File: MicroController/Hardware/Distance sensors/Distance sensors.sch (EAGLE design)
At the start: 37 parts, among them U1 LM2937IMP-5.0, U2 TXB0108PWR, U3 TLV1117-33CDCY, U4 TXB0108PWR, X1 0446200002, X2 0446200002, X3 0446200002

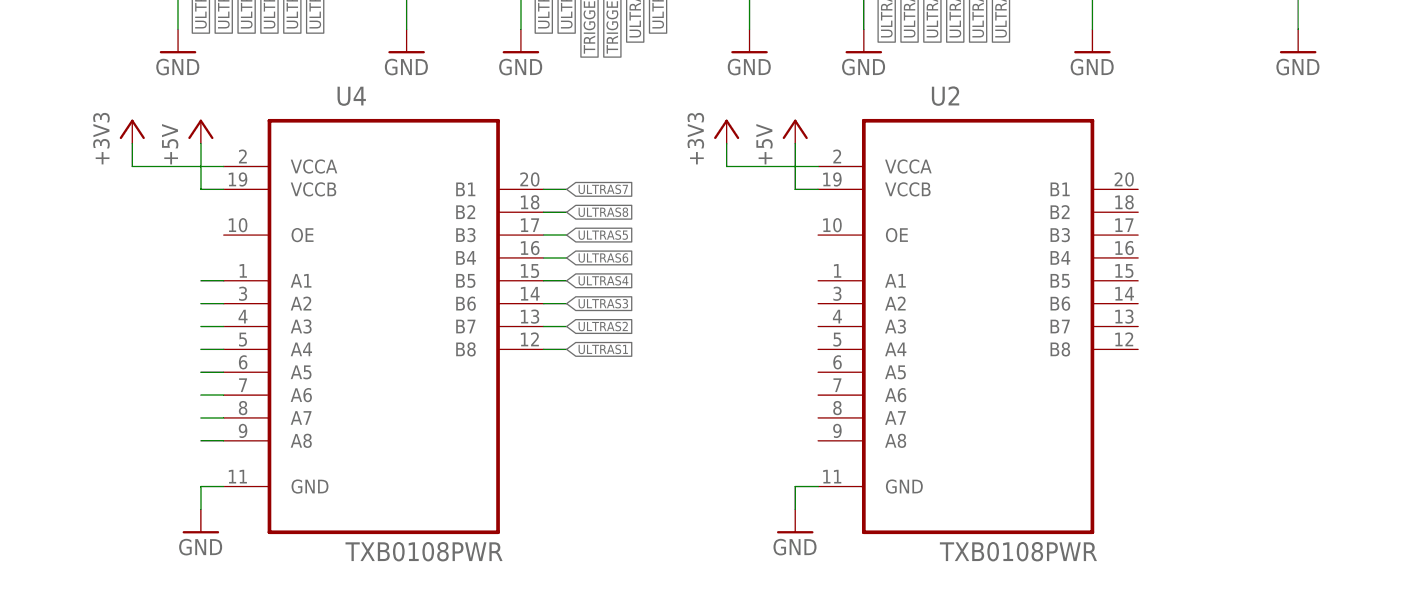
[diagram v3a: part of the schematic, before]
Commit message: Version with two 5V terminals.
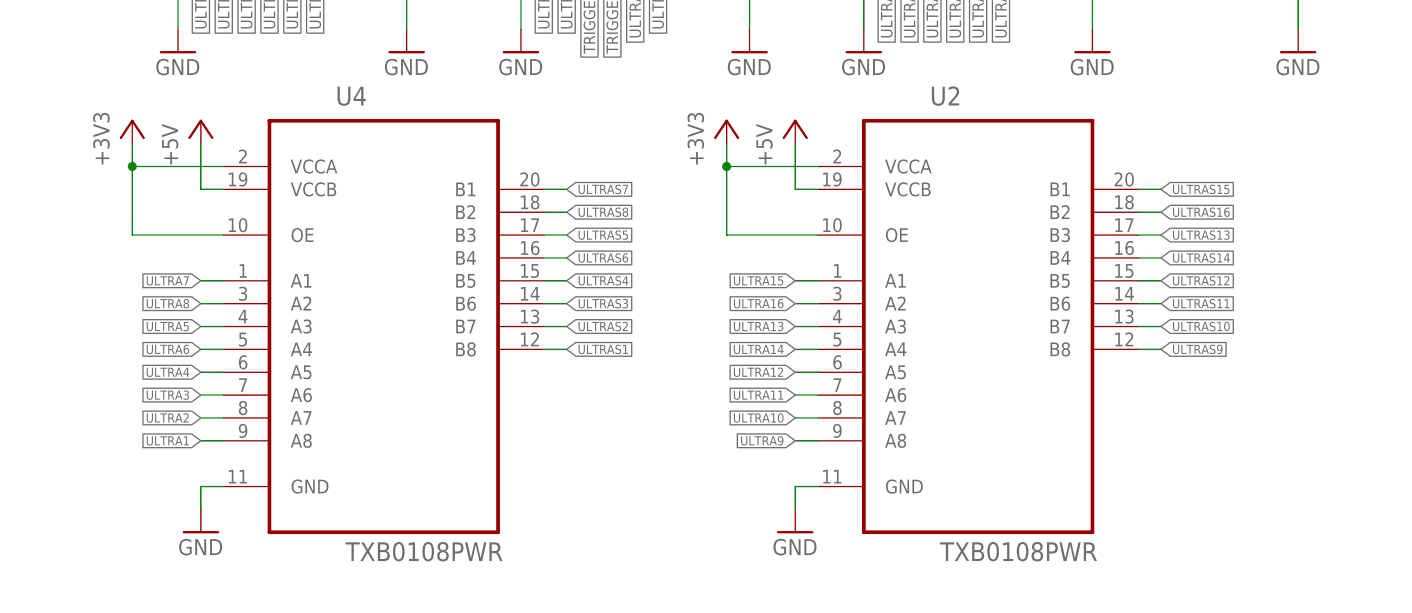
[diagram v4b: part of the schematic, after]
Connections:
- removed net N$1: U4.A1
- removed net N$2: U4.A2
- removed net N$3: U4.A3
- removed net N$4: U4.A4
- removed net N$5: U4.A5
- removed net N$6: U4.A6
- removed net N$7: U4.A7
- removed net N$8: U4.A8
- net +3V3: now also U2.OE, U4.OE
- net ULTRA1: now also U4.A8
- net ULTRA10: now also U2.A7
- net ULTRA11: now also U2.A6
- net ULTRA12: now also U2.A5
- net ULTRA13: now also U2.A3
- net ULTRA14: now also U2.A4
- net ULTRA15: now also U2.A1
- net ULTRA16: now also U2.A2
- net ULTRA2: now also U4.A7
- net ULTRA3: now also U4.A6
- net ULTRA4: now also U4.A5
- net ULTRA5: now also U4.A3
- net ULTRA6: now also U4.A4
- net ULTRA7: now also U4.A1
- net ULTRA8: now also U4.A2
- net ULTRA9: now also U2.A8
- net ULTRAS10: now also U2.B7
- net ULTRAS11: now also U2.B6
- net ULTRAS12: now also U2.B5
- net ULTRAS13: now also U2.B3
- net ULTRAS14: now also U2.B4
- net ULTRAS15: now also U2.B1
- net ULTRAS16: now also U2.B2
- net ULTRAS9: now also U2.B8

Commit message: Changed to one 4-pin connector for each sensor.
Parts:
- removed 5V, J1: (no value), SparkFun-Connectors:CONN_022.54MM_SCREWTERM
- removed SENSOR_1, SENSOR_10, SENSOR_11, SENSOR_12, SENSOR_13, SENSOR_14, SENSOR_15, SENSOR_16, SENSOR_2, SENSOR_3, SENSOR_4, SENSOR_5, SENSOR_6, SENSOR_7, SENSOR_8, SENSOR_9: JST-PH_2-PIN_HEADER, SRG:JST-PH_2-PIN_HEADER
- added SEN1, SEN10, SEN11, SEN12, SEN13, SEN14, SEN15, SEN16, SEN2, SEN3, SEN4, SEN5, SEN6, SEN7, SEN8, SEN9: JST-PH_4-PIN_HEADER, SRG:JST-PH_4-PIN_HEADER
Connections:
- net +5V: now also SEN1.4, SEN10.4, SEN11.4, SEN12.4, SEN13.4, SEN14.4, SEN15.4, SEN16.4, SEN2.4, SEN3.4, SEN4.4, SEN5.4, SEN6.4, SEN7.4, SEN8.4, SEN9.4; no longer 5V.2, J1.1
- net GND: now also SEN1.1, SEN10.1, SEN11.1, SEN12.1, SEN13.1, SEN14.1, SEN15.1, SEN16.1, SEN2.1, SEN3.1, SEN4.1, SEN5.1, SEN6.1, SEN7.1, SEN8.1, SEN9.1; no longer 5V.1, J1.2
- net TRIGGER_1: now also SEN1.3, SEN2.3, SEN3.3, SEN4.3, SEN5.3, SEN6.3, SEN7.3, SEN8.3; no longer SENSOR_1.2, SENSOR_2.2, SENSOR_3.2, SENSOR_4.2, SENSOR_5.2, SENSOR_6.2, SENSOR_7.2, SENSOR_8.2
- net TRIGGER_2: now also SEN10.3, SEN11.3, SEN12.3, SEN13.3, SEN14.3, SEN15.3, SEN16.3, SEN9.3; no longer SENSOR_10.2, SENSOR_11.2, SENSOR_12.2, SENSOR_13.2, SENSOR_14.2, SENSOR_15.2, SENSOR_16.2, SENSOR_9.2
- net ULTRAS1: now also SEN1.2; no longer SENSOR_1.1
- net ULTRAS10: now also SEN10.2; no longer SENSOR_10.1
- net ULTRAS11: now also SEN11.2; no longer SENSOR_11.1
- net ULTRAS12: now also SEN12.2; no longer SENSOR_12.1
- net ULTRAS13: now also SEN13.2; no longer SENSOR_13.1
- net ULTRAS14: now also SEN14.2; no longer SENSOR_14.1
- net ULTRAS15: now also SEN15.2; no longer SENSOR_15.1
- net ULTRAS16: now also SEN16.2; no longer SENSOR_16.1
- net ULTRAS2: now also SEN2.2; no longer SENSOR_2.1
- net ULTRAS3: now also SEN3.2; no longer SENSOR_3.1
- net ULTRAS4: now also SEN4.2; no longer SENSOR_4.1
- net ULTRAS5: now also SEN5.2; no longer SENSOR_5.1
- net ULTRAS6: now also SEN6.2; no longer SENSOR_6.1
- net ULTRAS7: now also SEN7.2; no longer SENSOR_7.1
- net ULTRAS8: now also SEN8.2; no longer SENSOR_8.1
- net ULTRAS9: now also SEN9.2; no longer SENSOR_9.1

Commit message: Finished the first version of the Ultrasone PCB.
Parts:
- added C10, C11, C12, C13: (no value), adafruit:C-USC0805
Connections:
- net +5V: now also C10.1, C11.1, C12.1, C13.1
- net GND: now also C10.2, C11.2, C12.2, C13.2
- net ULTRA13: now also U2.A4; no longer U2.A3
- net ULTRA14: now also U2.A3; no longer U2.A4
- net ULTRA15: now also U2.A2; no longer U2.A1
- net ULTRA16: now also U2.A1; no longer U2.A2
- net ULTRA5: now also U4.A4; no longer U4.A3
- net ULTRA6: now also U4.A3; no longer U4.A4
- net ULTRA7: now also U4.A2; no longer U4.A1
- net ULTRA8: now also U4.A1; no longer U4.A2
- net ULTRAS13: now also U2.B4; no longer U2.B3
- net ULTRAS14: now also U2.B3; no longer U2.B4
- net ULTRAS15: now also U2.B2; no longer U2.B1
- net ULTRAS16: now also U2.B1; no longer U2.B2
- net ULTRAS5: now also U4.B4; no longer U4.B3
- net ULTRAS6: now also U4.B3; no longer U4.B4
- net ULTRAS7: now also U4.B2; no longer U4.B1
- net ULTRAS8: now also U4.B1; no longer U4.B2

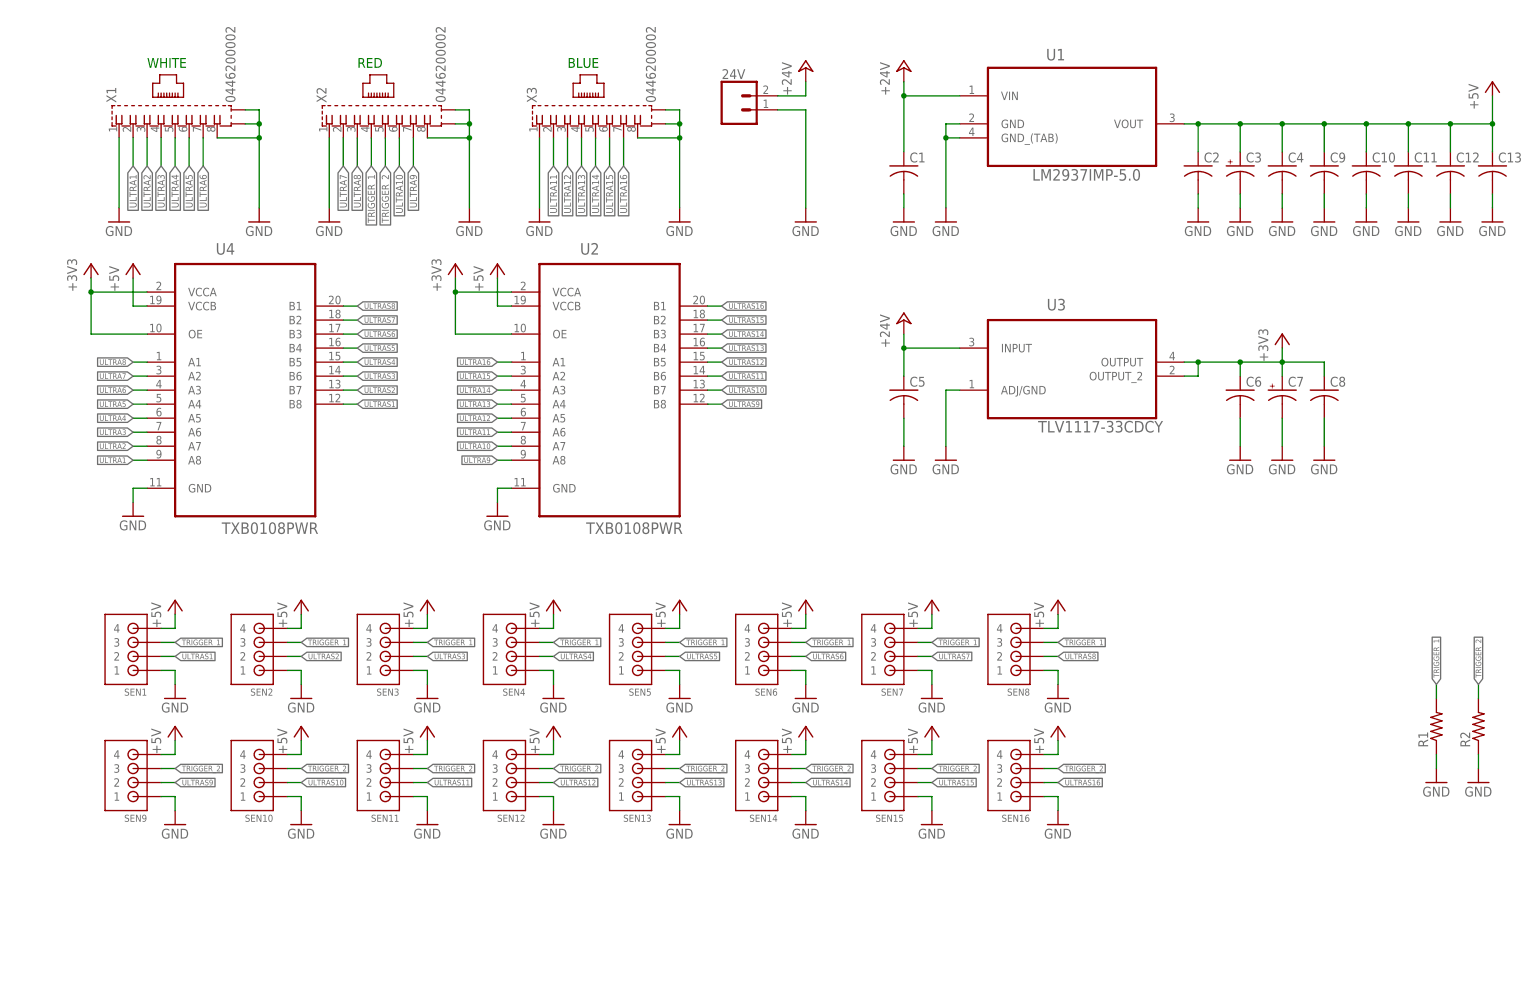
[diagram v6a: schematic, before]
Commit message: The distance sensor PCB is close to finished.
There needs to be a final check before ordering the PCB. The PCB is not very complicated compared to the previous version, making it easier to check.
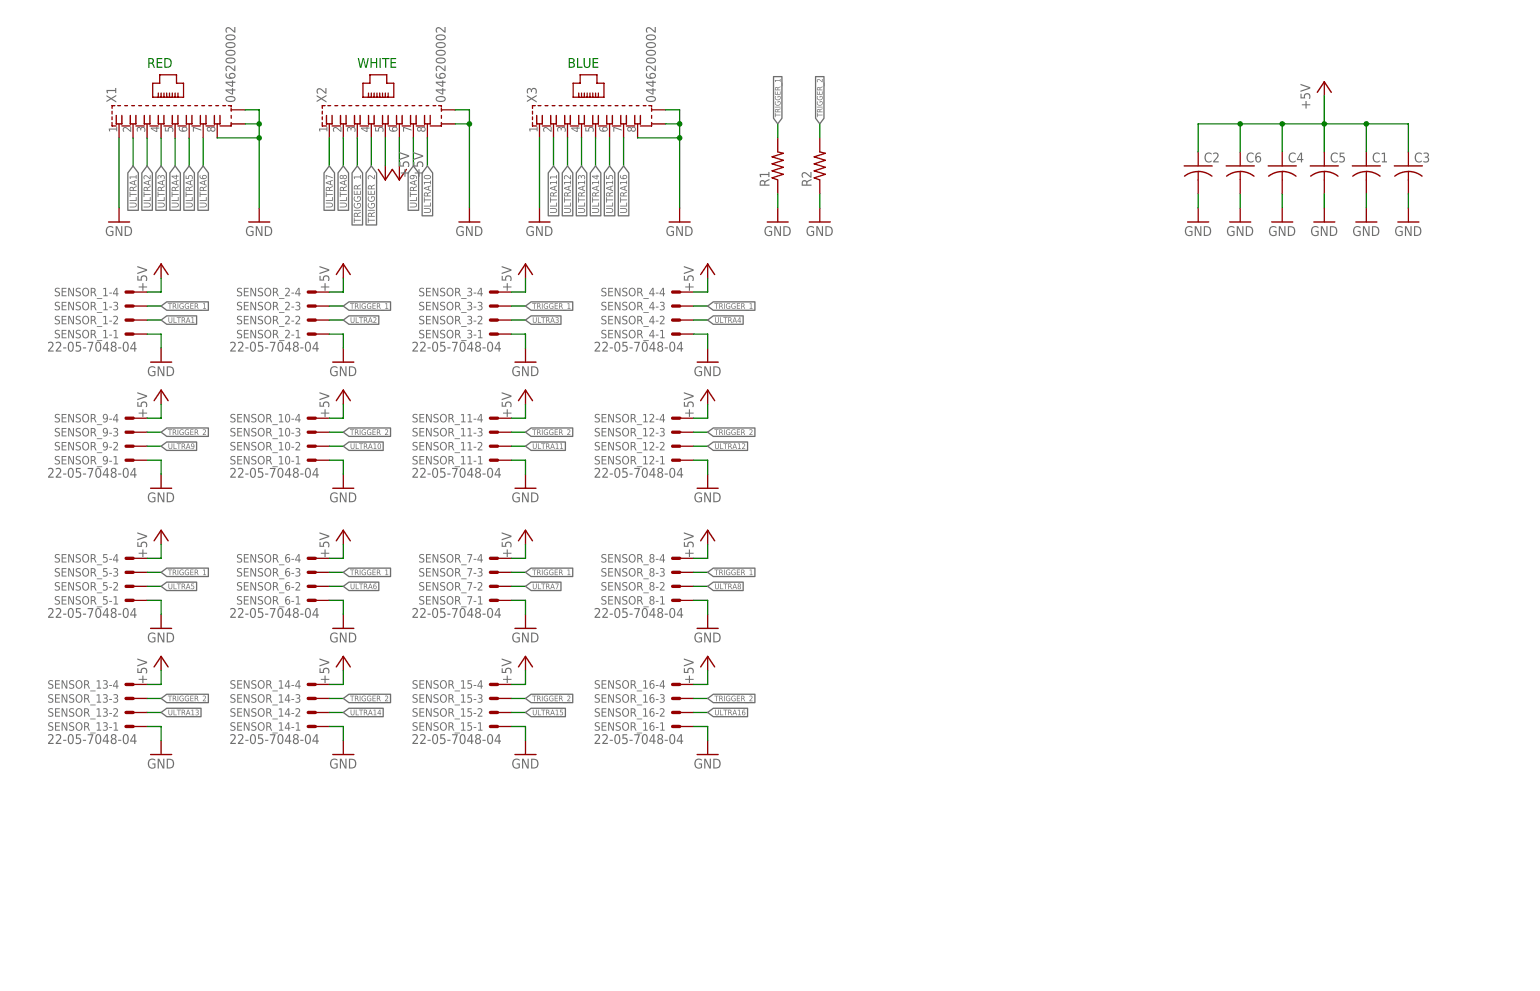
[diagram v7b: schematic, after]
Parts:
- removed 24V: (no value), SparkFun-Connectors:CONN_023.5MM
- removed C10, C11, C12, C13, C8, C9: (no value), adafruit:C-USC0805
- removed C7: (no value), adafruit:CPOL-US153CLV-0505
- removed SEN1, SEN10, SEN11, SEN12, SEN13, SEN14, SEN15, SEN16, SEN2, SEN3, SEN4, SEN5, SEN6, SEN7, SEN8, SEN9: JST-PH_4-PIN_HEADER, SRG:JST-PH_4-PIN_HEADER
- removed U1: LM2937IMP-5.0, NSC_By_element14_Batch_1.1:LM2937IMP-5.0
- removed U2, U4: TXB0108PWR, Texas Instruments_By_element14_Batch_1:TXB0108PWR
- removed U3: TLV1117-33CDCY, Texas Instruments_By_element14_Batch_1:TLV1117-33CDCY
- added SENSOR_1, SENSOR_10, SENSOR_11, SENSOR_12, SENSOR_13, SENSOR_14, SENSOR_15, SENSOR_16, SENSOR_2, SENSOR_3, SENSOR_4, SENSOR_5, SENSOR_6, SENSOR_7, SENSOR_8, SENSOR_9: 22-05-7048-04, con-molex:22-05-7048-04
- C1, C5: device adafruit:C-USC1206 -> adafruit:C-USC0805
- C3: device adafruit:CPOL-US153CLV-0505 -> adafruit:C-USC1206
- C6: device adafruit:C-USC0805 -> adafruit:C-USC1206
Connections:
- removed net +24V: 24V.2, C1.1, C5.1, U1.VIN, U3.INPUT
- removed net +3V3: C6.1, C7.+, C8.1, U2.OE, U2.VCCA, U3.OUTPUT, U3.OUTPUT_2, U4.OE, U4.VCCA
- removed net ULTRAS1: SEN1.2, U4.B8
- removed net ULTRAS10: SEN10.2, U2.B7
- removed net ULTRAS11: SEN11.2, U2.B6
- removed net ULTRAS12: SEN12.2, U2.B5
- removed net ULTRAS13: SEN13.2, U2.B4
- removed net ULTRAS14: SEN14.2, U2.B3
- removed net ULTRAS15: SEN15.2, U2.B2
- removed net ULTRAS16: SEN16.2, U2.B1
- removed net ULTRAS2: SEN2.2, U4.B7
- removed net ULTRAS3: SEN3.2, U4.B6
- removed net ULTRAS4: SEN4.2, U4.B5
- removed net ULTRAS5: SEN5.2, U4.B4
- removed net ULTRAS6: SEN6.2, U4.B3
- removed net ULTRAS7: SEN7.2, U4.B2
- removed net ULTRAS8: SEN8.2, U4.B1
- removed net ULTRAS9: SEN9.2, U2.B8
- net +5V: now also C1.1, C3.1, C5.1, C6.1, SENSOR_1-4.S, SENSOR_10-4.S, SENSOR_11-4.S, SENSOR_12-4.S, SENSOR_13-4.S, SENSOR_14-4.S, SENSOR_15-4.S, SENSOR_16-4.S, SENSOR_2-4.S, SENSOR_3-4.S, SENSOR_4-4.S, SENSOR_5-4.S, SENSOR_6-4.S, SENSOR_7-4.S, SENSOR_8-4.S, SENSOR_9-4.S, X2.5, X2.6; no longer C10.1, C11.1, C12.1, C13.1, C3.+, C9.1, SEN1.4, SEN10.4, SEN11.4, SEN12.4, SEN13.4, SEN14.4, SEN15.4, SEN16.4, SEN2.4, SEN3.4, SEN4.4, SEN5.4, SEN6.4, SEN7.4, SEN8.4, SEN9.4, U1.VOUT, U2.VCCB, U4.VCCB
- net GND: now also C3.2, SENSOR_1-1.S, SENSOR_10-1.S, SENSOR_11-1.S, SENSOR_12-1.S, SENSOR_13-1.S, SENSOR_14-1.S, SENSOR_15-1.S, SENSOR_16-1.S, SENSOR_2-1.S, SENSOR_3-1.S, SENSOR_4-1.S, SENSOR_5-1.S, SENSOR_6-1.S, SENSOR_7-1.S, SENSOR_8-1.S, SENSOR_9-1.S; no longer 24V.1, C10.2, C11.2, C12.2, C13.2, C3.-, C7.-, C8.2, C9.2, SEN1.1, SEN10.1, SEN11.1, SEN12.1, SEN13.1, SEN14.1, SEN15.1, SEN16.1, SEN2.1, SEN3.1, SEN4.1, SEN5.1, SEN6.1, SEN7.1, SEN8.1, SEN9.1, U1.GND, U1.GND_(TAB), U2.GND, U3.ADJ/GND, U4.GND, X2.1, X2.8
- net TRIGGER_1: now also SENSOR_1-3.S, SENSOR_2-3.S, SENSOR_3-3.S, SENSOR_4-3.S, SENSOR_5-3.S, SENSOR_6-3.S, SENSOR_7-3.S, SENSOR_8-3.S, X2.3; no longer SEN1.3, SEN2.3, SEN3.3, SEN4.3, SEN5.3, SEN6.3, SEN7.3, SEN8.3, X2.4
- net TRIGGER_2: now also SENSOR_10-3.S, SENSOR_11-3.S, SENSOR_12-3.S, SENSOR_13-3.S, SENSOR_14-3.S, SENSOR_15-3.S, SENSOR_16-3.S, SENSOR_9-3.S, X2.4; no longer SEN10.3, SEN11.3, SEN12.3, SEN13.3, SEN14.3, SEN15.3, SEN16.3, SEN9.3, X2.5
- net ULTRA1: now also SENSOR_1-2.S; no longer U4.A8
- net ULTRA10: now also SENSOR_10-2.S, X2.8; no longer U2.A7, X2.6
- net ULTRA11: now also SENSOR_11-2.S; no longer U2.A6
- net ULTRA12: now also SENSOR_12-2.S; no longer U2.A5
- net ULTRA13: now also SENSOR_13-2.S; no longer U2.A4
- net ULTRA14: now also SENSOR_14-2.S; no longer U2.A3
- net ULTRA15: now also SENSOR_15-2.S; no longer U2.A2
- net ULTRA16: now also SENSOR_16-2.S; no longer U2.A1
- net ULTRA2: now also SENSOR_2-2.S; no longer U4.A7
- net ULTRA3: now also SENSOR_3-2.S; no longer U4.A6
- net ULTRA4: now also SENSOR_4-2.S; no longer U4.A5
- net ULTRA5: now also SENSOR_5-2.S; no longer U4.A4
- net ULTRA6: now also SENSOR_6-2.S; no longer U4.A3
- net ULTRA7: now also SENSOR_7-2.S, X2.1; no longer U4.A2, X2.2
- net ULTRA8: now also SENSOR_8-2.S, X2.2; no longer U4.A1, X2.3
- net ULTRA9: now also SENSOR_9-2.S; no longer U2.A8
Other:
- moved on the sheet: C1, C5, C6, R1, R2
